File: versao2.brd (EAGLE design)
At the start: 77.7 x 64.9 mm, 22 parts

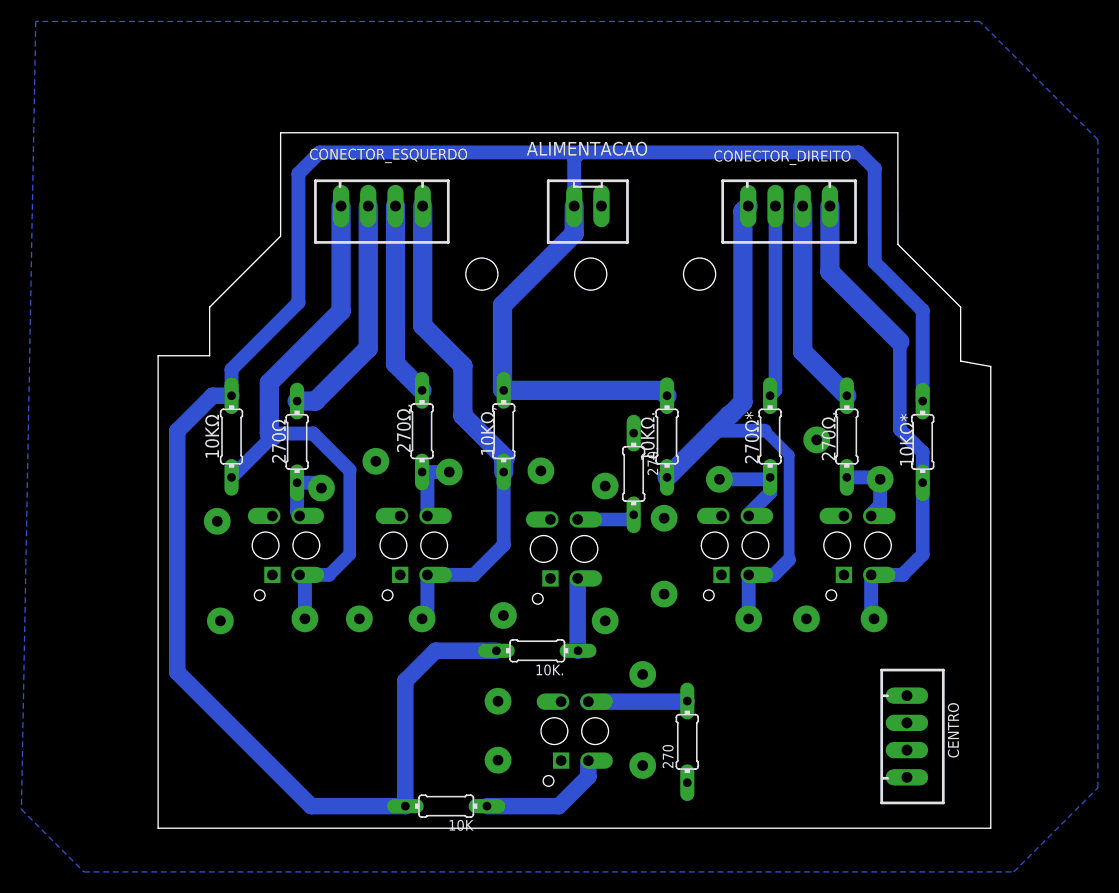
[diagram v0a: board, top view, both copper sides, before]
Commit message: organizacao da placa com 6 sensores
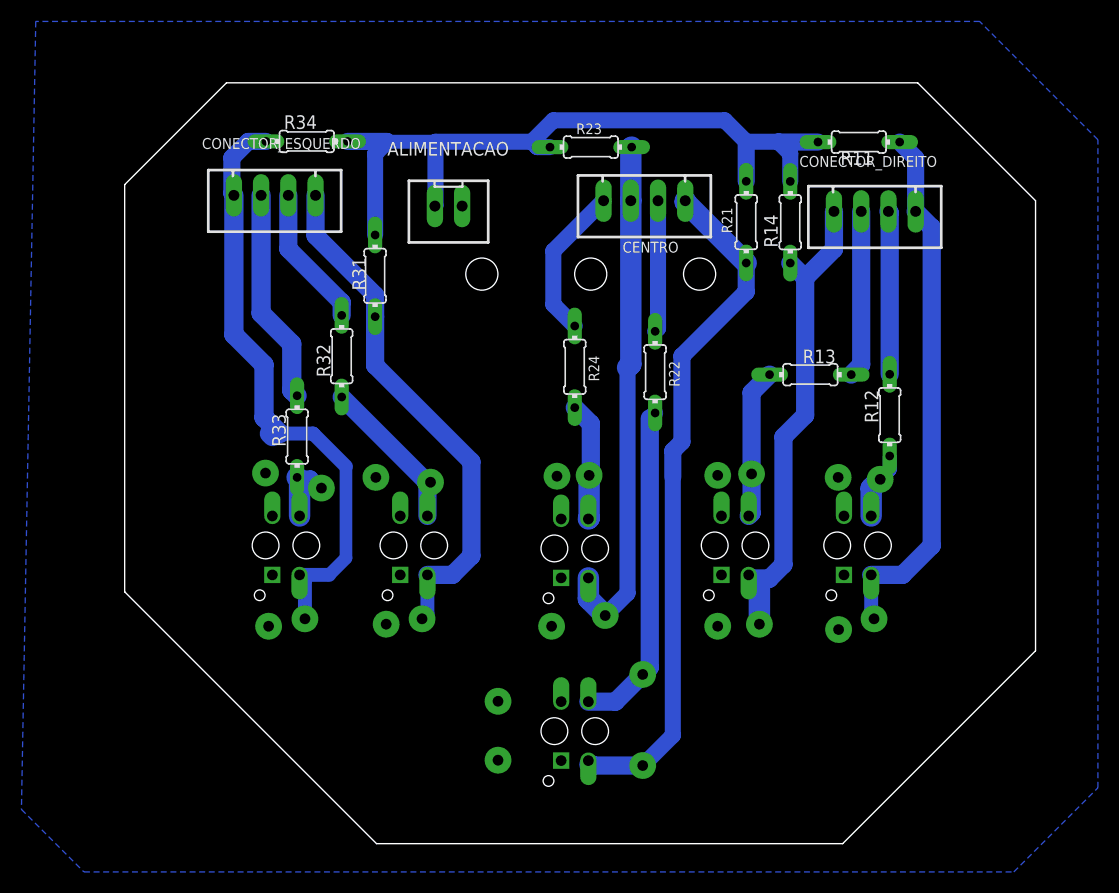
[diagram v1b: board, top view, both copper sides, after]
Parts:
- removed 10K, 10K., 10KΩ, 10KΩ*, 10KΩ,, 10KΩ.: 10KΩ, rcl_robotica:0204/7
- removed 270, 270., 270Ω, 270Ω*, 270Ω,, 270Ω.: 270Ω, rcl_robotica:0204/7
- added R11, R14, R21, R23, R31, R34: 10KΩ, rcl_robotica:0204/7
- added R12, R13, R22, R24, R32, R33: 270Ω, rcl_robotica:0204/7
- moved CENTRO 55.7 mm to (52.0, 64.0), turned to 180 degrees
- moved ALIMENTACAO 13.0 mm to (33.7, 63.5)
- moved CONECTOR_ESQUERDO 10.0 mm to (17.5, 64.5)
- moved CONECTOR_DIREITO 8.02 mm to (73.5, 63.0)
- moved CENTRAL 1.00 mm to (45.5, 31.6)
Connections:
- new net N$10: CENTRO.4, R24.1
- new net N$5: CENTRO.2, R22.1
- net +5V: now also R11.2, R14.2, R21.2, R23.2, R31.2, R34.2; no longer 10K..2, 10K.2, 10KΩ*.2, 10KΩ,.2, 10KΩ..2, 10KΩ.2
- net ANALOG_+DI: now also R11.1; no longer 10KΩ*.1
- net ANALOG_+ESQ.: now also R34.1; no longer 10KΩ.1
- net ANALOG_DI: now also R14.1; no longer 10KΩ..1
- net ANALOG_ESQ: now also R31.1; no longer 10KΩ,.1
- net DIGITAL+ESQ.: now also R33.1; no longer 270Ω.1
- net DIGITAL_+DI: now also R12.1; no longer 270Ω,.1
- net DIGITAL_DI: now also R13.1; no longer 270Ω*.1
- net DIGITAL_ESQ.: now also R32.1; no longer 270Ω..1
- net N$1: now also R33.2; no longer 270Ω.2
- net N$2: now also R32.2; no longer 270Ω..2
- net N$3: now also R13.2; no longer 270Ω*.2
- net N$4: now also R12.2; no longer 270Ω,.2
- net N$6: now also CENTRO.3, R23.1; no longer 10K..1
- net N$7: now also R24.2; no longer 270..2
- net N$8: now also CENTRO.1, R21.1; no longer 10K.1
- net N$9: now also R22.2; no longer 270.2
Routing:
- net +5V: track 219.6 -> 70.5 mm
- net N$8: track 12.1 -> 64.5 mm, vias 0 -> 1
- net N$6: track 6.48 -> 50.6 mm, vias 0 -> 1
- net N$9: track 9.25 -> 31.0 mm, vias 0 -> 1
- net N$10: track 0.00 -> 14.5 mm
- net N$5: track 0.00 -> 12.3 mm
- net N$2: track 6.68 -> 14.8 mm
- net ANALOG_DI: track 54.5 -> 47.1 mm
- net N$7: track 5.41 -> 11.1 mm, vias 0 -> 1
- net DIGITAL_ESQ.: track 18.2 -> 13.3 mm
- net N$3: track 9.07 -> 14.0 mm
- net DIGITAL_+DI: track 19.4 -> 15.2 mm
- net ANALOG_+DI: track 46.3 -> 50.0 mm
- net DIGITAL_DI: track 17.9 -> 15.6 mm
- net DIGITAL+ESQ.: track 22.0 -> 20.1 mm
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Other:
- board size 77.7 x 64.9 mm -> 85 x 71 mm

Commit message: adicionando os arquivos da placa de refletancia com 6 sensores.
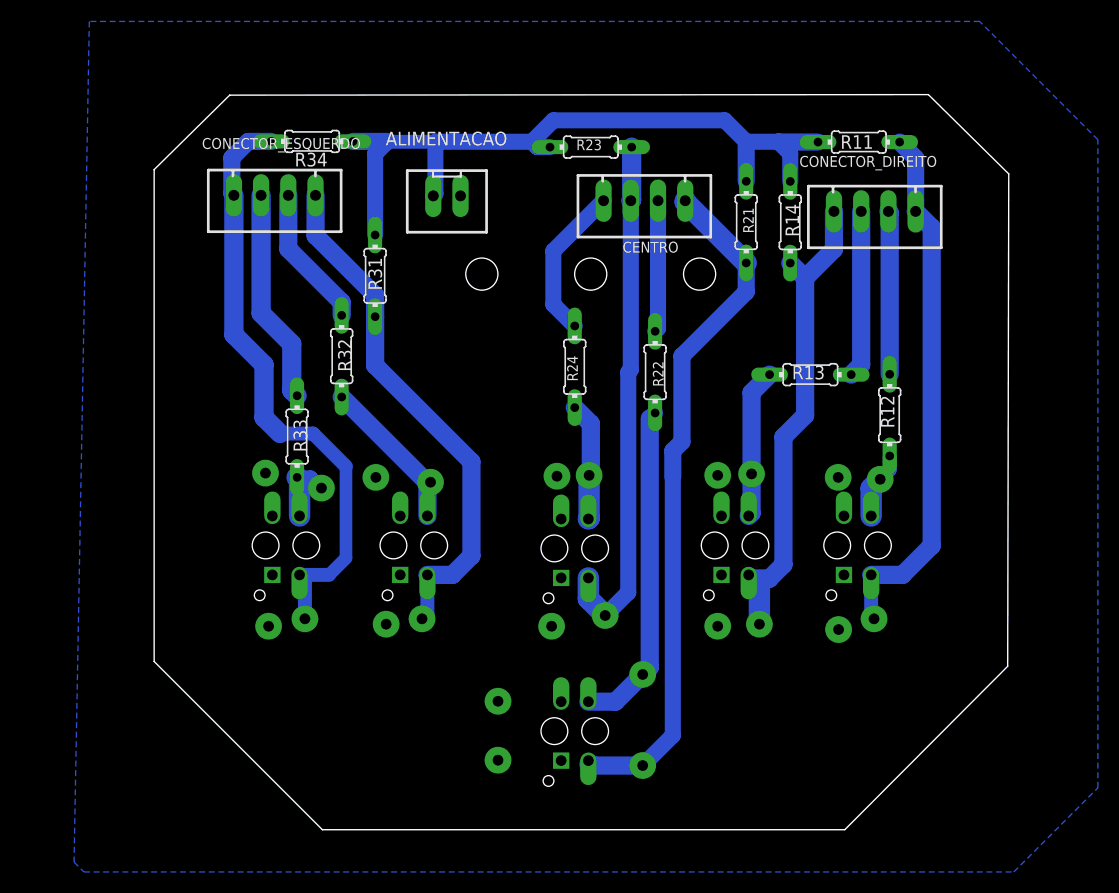
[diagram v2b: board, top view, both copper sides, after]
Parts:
- moved ALIMENTACAO 0.96 mm to (33.6, 64.5)
- moved R34 0.50 mm to (21.0, 69.5)
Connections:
- net ANALOG_+ESQ. renamed ANALOG+ESQ
- net DIGITAL+ESQ. renamed DIGITAL+ESQ
- net DIGITAL_ESQ. renamed DIGITAL_ESQ
- net N$1 renamed DIGITA+ESQ
- net N$10 renamed DIGITAL_CE
- net N$2 renamed DIGITAL
- net N$3 renamed DIGTAL-DI
- net N$4 renamed DIGITAL+DIR
- net N$5 renamed FRONTAL
- net N$6 renamed ANALOG_CE
- net N$7 renamed CENTRAL
- net N$8 renamed ANALOG_FR
- net N$9 renamed DIGITAL_FR
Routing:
- net ANALOG_CE: track 50.6 -> 48.9 mm
- net ANALOG+ESQ: track 58.8 -> 57.2 mm
- net +5V: track 70.5 -> 69.1 mm
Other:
- board size 85 x 71 mm -> 79.8 x 68.6 mm
